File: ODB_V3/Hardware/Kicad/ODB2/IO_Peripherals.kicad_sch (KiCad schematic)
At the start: 13 parts, among them IC1 W25Q512JVEIQ, J3 SYS_SW_Conn_01x05_Header, J6 RFD_Conn_01x05_Header

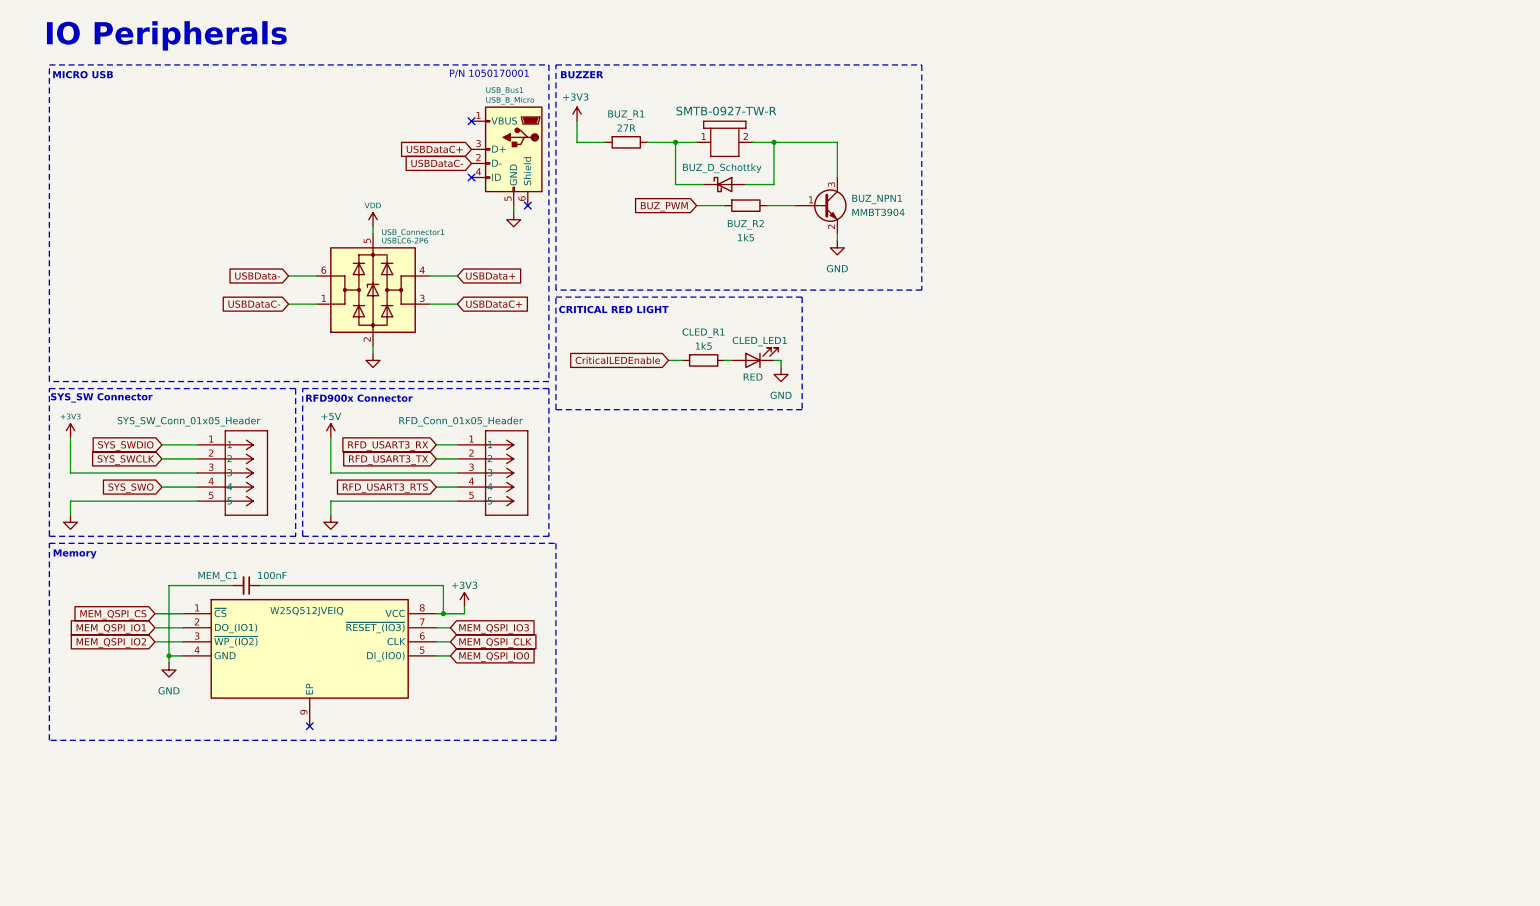
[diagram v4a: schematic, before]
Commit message: feat: add mem2067
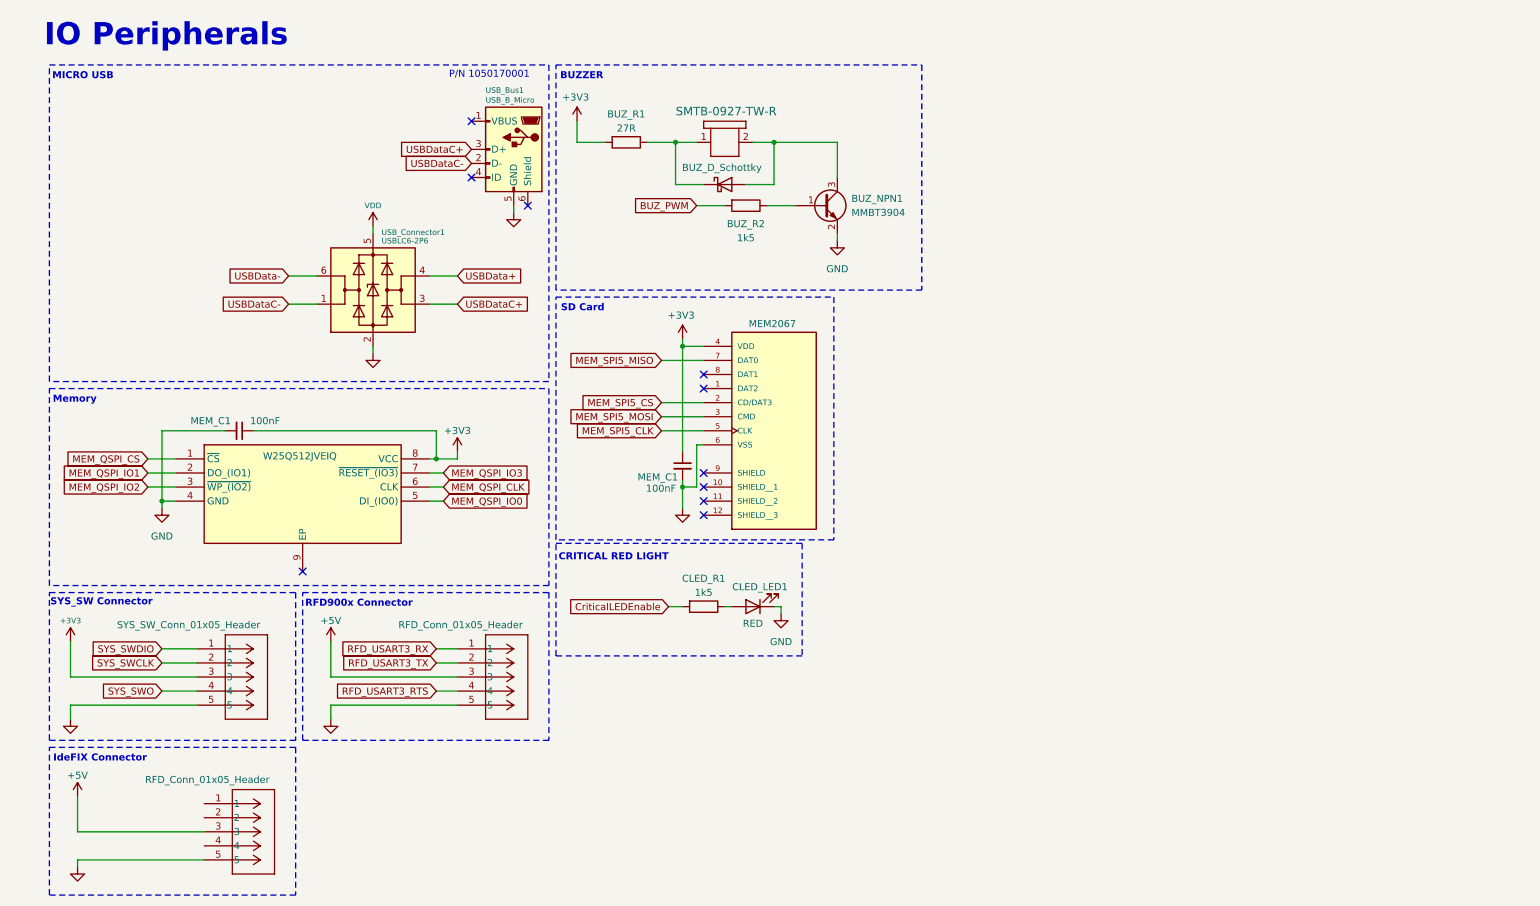
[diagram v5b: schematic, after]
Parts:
- added J2: RFD_Conn_01x05_Header, ODB:CONN_SDA-70543-xxxx_05_MOL, symbol ODB2:705430004
- added J5: MEM2067, MEM2067-02-180-00-A_REVB:GCT_MEM2067-02-180-00-A_REVB, symbol ODB2:MEM2067
- added MEM_C1: 100nF, Capacitor_SMD:C_0603_1608Metric, symbol Device:C_Small
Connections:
- net +3V3: now also J5.4 (VDD), MEM_C1.1
- net +5V: now also J2.3
- net GND: now also J2.5, J5.6 (VSS), MEM_C1.2
- new net MEM_SPI5_CLK: J5.5 (CLK)
- new net MEM_SPI5_CS: J5.2 (CD/DAT3)
- new net MEM_SPI5_MISO: J5.7 (DAT0)
- new net MEM_SPI5_MOSI: J5.3 (CMD)
- no-connect marks 4 -> 10
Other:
- note added: "IdeFIX Connector"
- note added: "SD Card"
- moved on the sheet: CLED_LED1, CLED_R1, MEM_C1

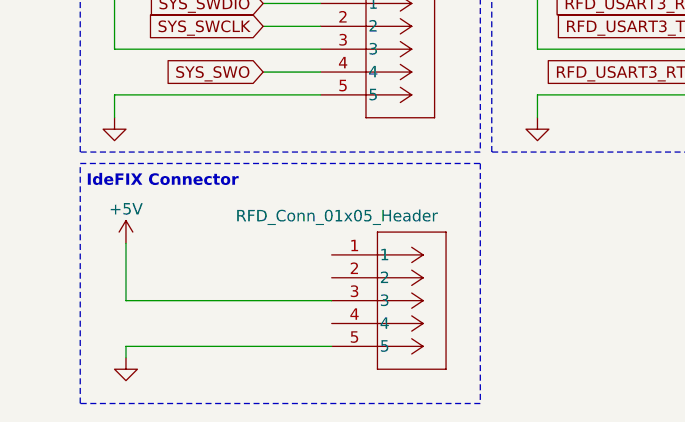
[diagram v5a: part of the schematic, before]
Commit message: feat: add IdeFIX I2C connector (4 pins)
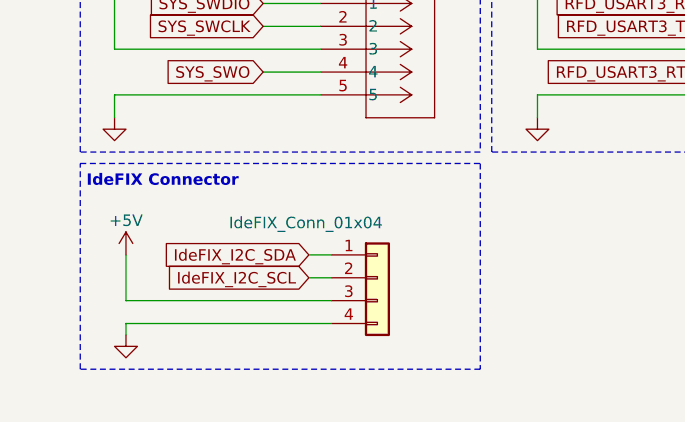
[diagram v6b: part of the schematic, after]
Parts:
- removed J2: RFD_Conn_01x05_Header, ODB:CONN_SDA-70543-xxxx_05_MOL, symbol ODB2:705430004
- added J2: IdeFIX_Conn_01x04, symbol Connector_Generic:Conn_01x04
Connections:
- net +5V: now also J2.3 (Pin_3)
- net GND: now also J2.4 (Pin_4)
- new net IdeFIX_I2C_SCL: J2.2 (Pin_2)
- new net IdeFIX_I2C_SDA: J2.1 (Pin_1)
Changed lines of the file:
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@@
 	(rectangle
 		(start 13.97 144.78)
-		(end 58.42 171.45)
+		(end 58.42 167.64)
 		(stroke
 			(width 0)
@@
 	(wire
 		(pts
-			(xy 19.05 165.1) (xy 19.05 166.37)
+			(xy 19.05 162.56) (xy 19.05 163.83)
 		)
 		(stroke
@@
 	(wire
 		(pts
-			(xy 41.91 165.1) (xy 19.05 165.1)
+			(xy 41.91 162.56) (xy 19.05 162.56)
 		)
 		(stroke
@@
 	(wire
 		(pts
+			(xy 39.37 157.48) (xy 41.91 157.48)
+		)
+		(stroke
+			(width 0)
+			(type default)
+		)
+	)
+	(wire
+		(pts
 			(xy 87.63 137.16) (xy 64.77 137.16)
 		)
@@
 	(wire
 		(pts
+			(xy 39.37 154.94) (xy 41.91 154.94)
+		)
+		(stroke
+			(width 0)
+			(type default)
+		)
+	)
+	(wire
+		(pts
 			(xy 128.27 96.52) (xy 128.27 97.79)
 		)
@@
 	(wire
 		(pts
-			(xy 19.05 153.67) (xy 19.05 160.02)
+			(xy 19.05 154.94) (xy 19.05 160.02)
 		)
 		(stroke
@@
 	(wire
 		(pts
+			(xy 19.05 160.02) (xy 41.91 160.02)
+		)
+		(stroke
+			(width 0)
+			(type default)
+		)
+	)
+	(wire
+		(pts
 			(xy 34.29 134.62) (xy 40.64 134.62)
 		)
@@
 		)
 	)
-	(wire
-		(pts
-			(xy 19.05 160.02) (xy 41.91 160.02)
-		)
-		(stroke
-			(width 0)
-			(type default)
-		)
-	)
 	(global_label "BUZ_PWM"
 		(shape input)
@@
 		)
 	)
+	(global_label "IdeFIX_I2C_SCL"
+		(shape input)
+		(at 39.37 157.48 180)
+		(fields_autoplaced yes)
+		(effects
+			(font
+				(size 1.27 1.27)
+			)
+			(justify right)
+		)
+		(property "Intersheetrefs" "${INTERSHEET_REFS}"
+			(at 22.1124 157.48 0)
+			(effects
+				(font
+					(size 1.27 1.27)
+				)
+				(justify right)
+				(hide yes)
+			)
+		)
+	)
 	(global_label "RFD_USART3_RX"
 		(shape input)
@@
 		(property "Intersheetrefs" "${INTERSHEET_REFS}"
 			(at 15.2182 97.79 0)
+			(effects
+				(font
+					(size 1.27 1.27)
+				)
+				(justify right)
+				(hide yes)
+			)
+		)
+	)
+	(global_label "IdeFIX_I2C_SDA"
+		(shape input)
+		(at 39.37 154.94 180)
+		(fields_autoplaced yes)
+		(effects
+			(font
+				(size 1.27 1.27)
+			)
+			(justify right)
+		)
+		(property "Intersheetrefs" "${INTERSHEET_REFS}"
+			(at 22.0519 154.94 0)
 			(effects
 				(font
@@
 	)
 	(symbol
+		(lib_id "Connector_Generic:Conn_01x04")
+		(at 46.99 157.48 0)
+		(unit 1)
+		(exclude_from_sim no)
+		(in_bom yes)
+		(on_board yes)
+		(dnp no)
+		(property "Reference" "J2"
+			(at 49.53 157.4799 0)
+			(effects
+				(font
+					(size 1.27 1.27)
+				)
+				(justify left)
+				(hide yes)
+			)
+		)
+		(property "Value" "IdeFIX_Conn_01x04"
+			(at 30.48 151.384 0)
+			(effects
+				(font
+					(size 1.27 1.27)
+				)
+				(justify left)
+			)
+		)
+		(property "Footprint" ""
+			(at 46.99 157.48 0)
+			(effects
+				(font
+					(size 1.27 1.27)
+				)
+				(hide yes)
+			)
+		)
+		(property "Datasheet" "~"
+			(at 46.99 157.48 0)
+			(effects
+				(font
+					(size 1.27 1.27)
+				)
+				(hide yes)
+			)
+		)
+		(property "Description" "Generic connector, single row, 01x04, script generated (kicad-library-utils/schlib/autogen/connector/)"
+			(at 46.99 157.48 0)
+			(effects
+				(font
+					(size 1.27 1.27)
+				)
+				(hide yes)
+			)
+		)
+		(pin "3"
+		)
+		(pin "2"
+		)
+		(pin "4"
+		)
+		(pin "1"
+		)
+		(instances
+			(project ""
+				(path "/4b06c5d1-aa8b-48ed-8972-b43a60cfab78/93865dc8-71fa-4dc6-90ce-f5a9779dfd41"
+					(reference "J2")
+					(unit 1)
+				)
+			)
+		)
+	)
+	(symbol
 		(lib_id "ODB2:W25Q512JVEIQ")
 		(at 36.83 92.71 0)
@@
 	(symbol
 		(lib_id "power:+5V")
-		(at 19.05 153.67 0)
+		(at 19.05 154.94 0)
 		(unit 1)
 		(exclude_from_sim no)
@@
 		(dnp no)
 		(property "Reference" "#PWR053"
-			(at 19.05 157.48 0)
+			(at 19.05 158.75 0)
 			(effects
 				(font
@@
 		)
 		(property "Value" "+5V"
-			(at 19.05 149.86 0)
+			(at 19.05 151.13 0)
 			(effects
 				(font
@@
 		)
 		(property "Footprint" ""
-			(at 19.05 153.67 0)
+			(at 19.05 154.94 0)
 			(effects
 				(font
@@
 		)
 		(property "Datasheet" ""
-			(at 19.05 153.67 0)
+			(at 19.05 154.94 0)
 			(effects
 				(font
@@
 		)
 		(property "Description" "Power symbol creates a global label with name \"+5V\""
-			(at 19.05 153.67 0)
+			(at 19.05 154.94 0)
 			(effects
 				(font
@@
 	)
 	(symbol
-		(lib_id "ODB2:705430004")
-		(at 41.91 154.94 0)
-		(unit 1)
-		(exclude_from_sim no)
-		(in_bom yes)
-		(on_board yes)
-		(dnp no)
-		(property "Reference" "J2"
-			(at 43.434 148.082 0)
-			(effects
-				(font
-					(size 1.524 1.524)
-				)
-				(justify left)
-				(hide yes)
-			)
-		)
-		(property "Value" "RFD_Conn_01x05_Header"
-			(at 31.242 150.622 0)
-			(effects
-				(font
-					(size 1.27 1.27)
-				)
-				(justify left)
-			)
-		)
-		(property "Footprint" "ODB:CONN_SDA-70543-xxxx_05_MOL"
-			(at 32.004 148.336 0)
-			(effects
-				(font
-					(size 1.27 1.27)
-					(italic yes)
-				)
-				(hide yes)
-			)
-		)
-		(property "Datasheet" "705430004"
-			(at 60.706 151.384 0)
-			(effects
-				(font
-					(size 1.27 1.27)
-					(italic yes)
-				)
-				(hide yes)
-			)
-		)
-		(property "Description" ""
-			(at 41.91 154.94 0)
-			(effects
-				(font
-					(size 1.27 1.27)
-				)
-				(hide yes)
-			)
-		)
-		(pin "1"
-		)
-		(pin "5"
-		)
-		(pin "4"
-		)
-		(pin "2"
-		)
-		(pin "3"
-		)
-		(instances
-			(project "ODB2"
-				(path "/4b06c5d1-aa8b-48ed-8972-b43a60cfab78/93865dc8-71fa-4dc6-90ce-f5a9779dfd41"
-					(reference "J2")
-					(unit 1)
-				)
-			)
-		)
-	)
-	(symbol
 		(lib_name "+3V3_2")
 		(lib_id "power:+3V3")
@@
 	(symbol
 		(lib_id "power:GND")
-		(at 19.05 166.37 0)
+		(at 19.05 163.83 0)
 		(unit 1)
 		(exclude_from_sim no)
@@
 		(fields_autoplaced yes)
 		(property "Reference" "#PWR054"
-			(at 19.05 172.72 0)
+			(at 19.05 170.18 0)
 			(effects
 				(font
@@
 		)
 		(property "Value" "GND"
-			(at 19.05 171.45 0)
+			(at 19.05 168.91 0)
 			(effects
 				(font
@@
 		)
 		(property "Footprint" ""
-			(at 19.05 166.37 0)
+			(at 19.05 163.83 0)
 			(effects
 				(font
@@
 		)
 		(property "Datasheet" ""
-			(at 19.05 166.37 0)
+			(at 19.05 163.83 0)
 			(effects
 				(font
@@
 		)
 		(property "Description" ""
-			(at 19.05 166.37 0)
-			(effects
-				(font
+			(at 19.05 163.83 0)
+			(effects
+				(font

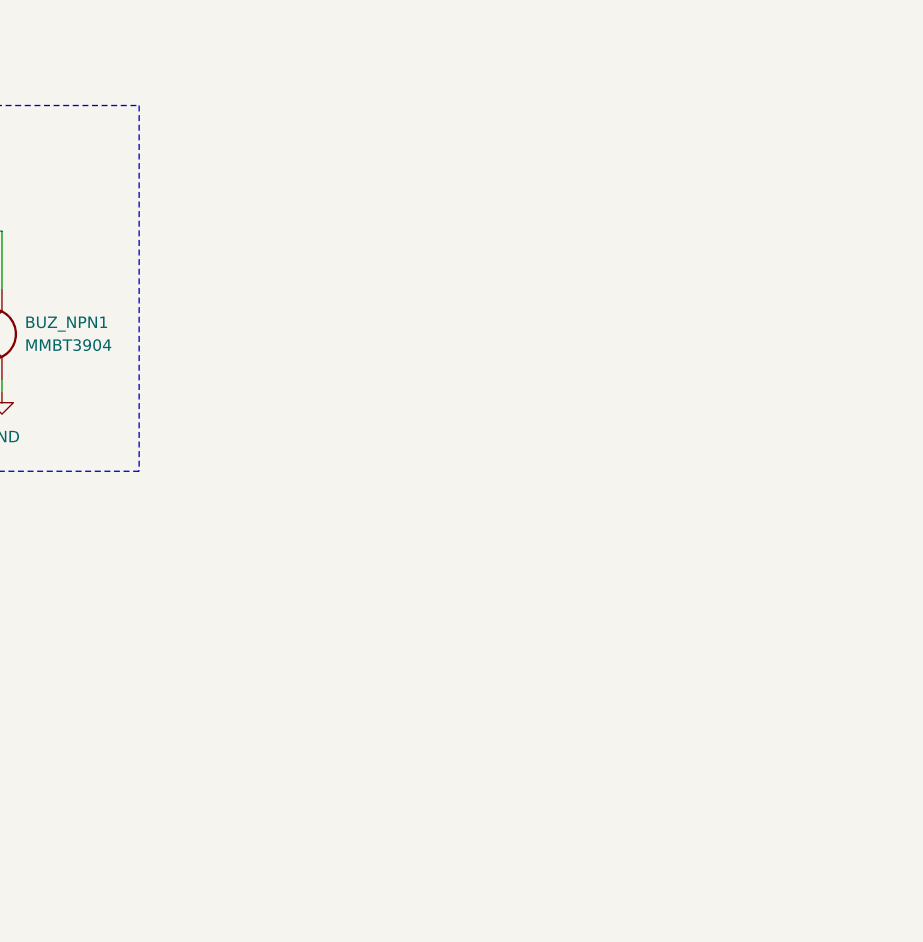
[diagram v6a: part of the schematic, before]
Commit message: fix: gps page remove
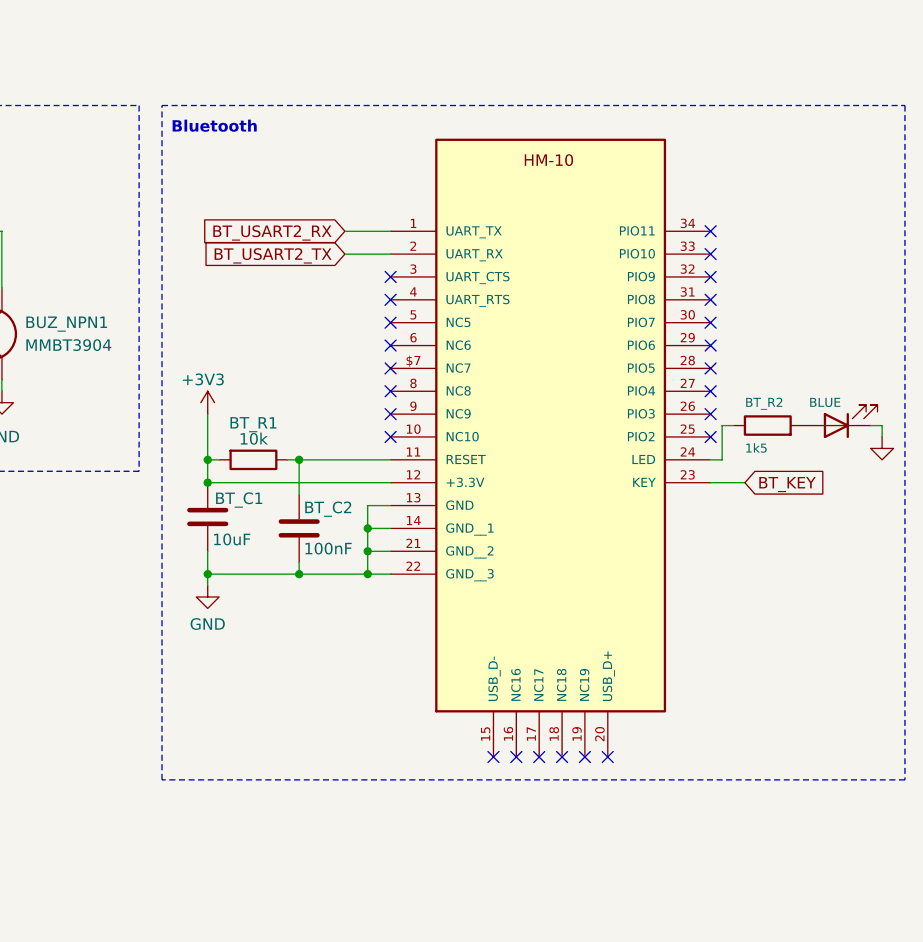
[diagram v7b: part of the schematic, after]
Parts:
- added BT_C1: 10uF, Capacitor_SMD:C_0603_1608Metric, symbol Device:C
- added BT_C2: 100nF, Capacitor_SMD:C_0603_1608Metric, symbol Device:C
- added BT_LED1: BLUE, LED_SMD:LED_0603_1608Metric, symbol Device:LED
- added BT_R1: 10k, Resistor_SMD:R_0603_1608Metric, symbol Device:R
- added BT_R2: 1k5, Resistor_SMD:R_0603_1608Metric, symbol Device:R
- added E1: HM-10, ODB:HM-10, symbol ODB_Lib:HM-10
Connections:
- net +3V3: now also BT_C1.1, BT_R1.2, E1.12 (+3.3V)
- net GND: now also BT_C1.2, BT_C2.2, BT_LED1.1 (K), E1.13 (GND), E1.14 (GND__1), E1.21 (GND__2), E1.22 (GND__3)
- new net: BT_LED1.2 (A), BT_R2.2
- new net: BT_C2.1, BT_R1.1, E1.11 (RESET)
- new net: BT_R2.1, E1.24 (LED)
- new net BT_KEY: E1.23 (KEY)
- new net BT_USART2_RX: E1.1 (UART_TX)
- new net BT_USART2_TX: E1.2 (UART_RX)
- no-connect marks 10 -> 34
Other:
- note added: "Bluetooth"
